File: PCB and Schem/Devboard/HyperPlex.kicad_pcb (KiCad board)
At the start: 2 copper layers, 23.2 x 47.8 mm, 27 parts, among them J1 USB_C_Receptacle_USB2.0_16P, Q1 2N3904, Q2 2N3904, Q3 2N3904, SW1 SW_Push, SW2 SW_SPDT, SW3 SW_SPDT, SW4 SW_Push, U1 CH32V203CxTx, U3 XC6206PxxxMR, U4 TP4056-42-ESOP8, U6 XC6206PxxxMR

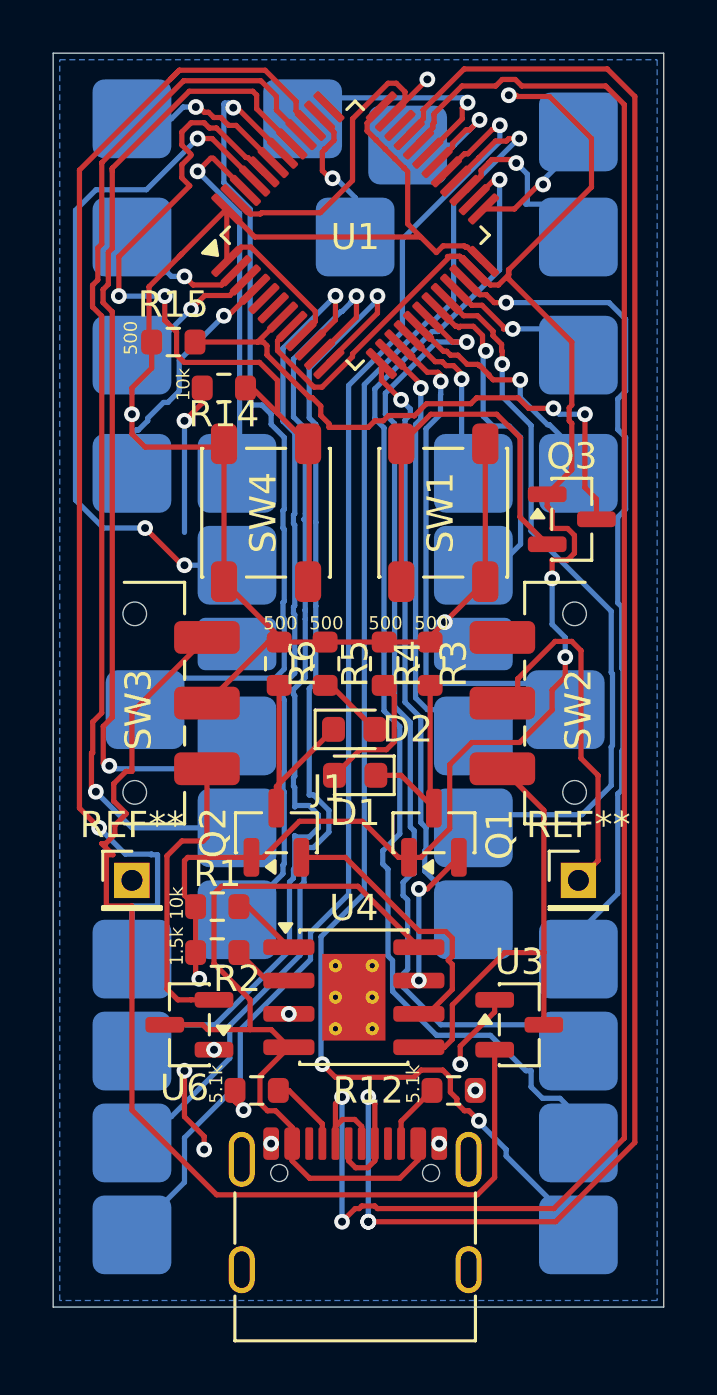
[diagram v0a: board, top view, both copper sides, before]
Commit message: Updated README, made Module 1 Schematic, started BOM
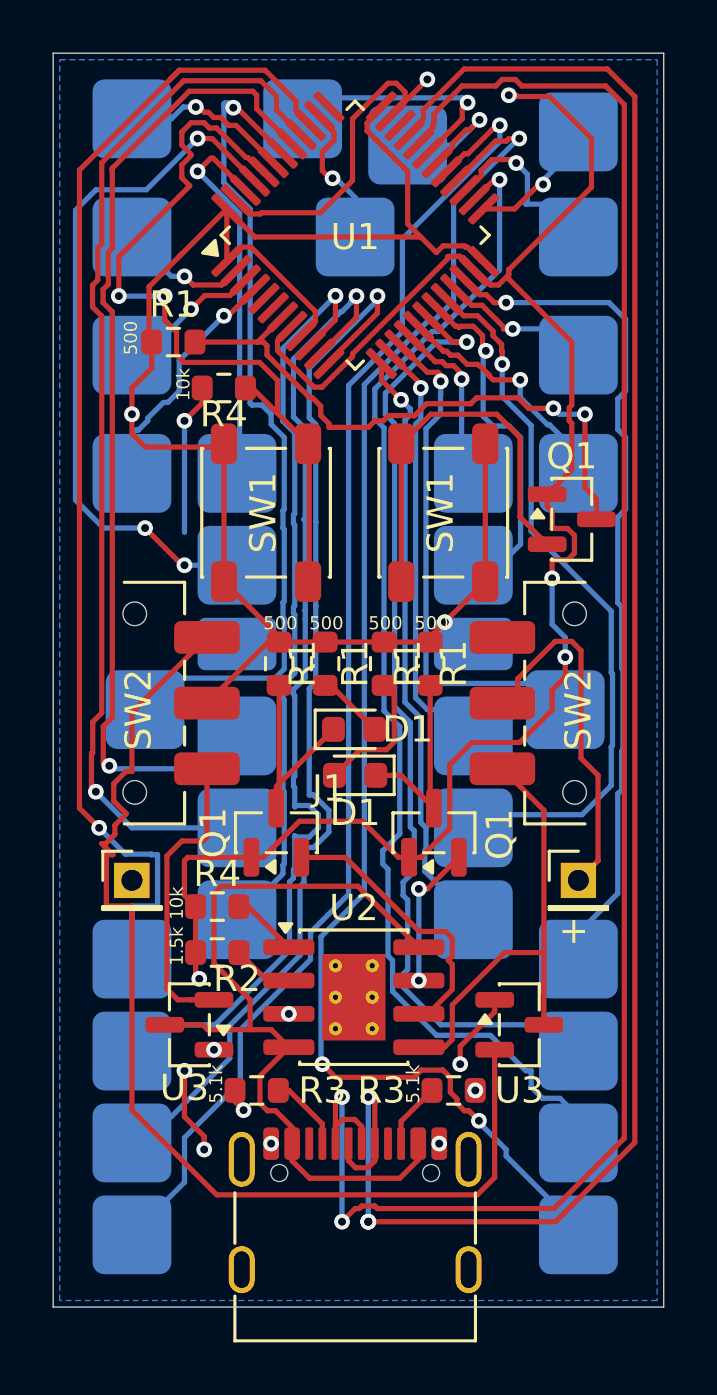
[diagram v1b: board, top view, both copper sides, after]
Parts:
- renumbered D2 to D1, Q2 to Q1, Q3 to Q1, R6 to R1, R5 to R1, R4 to R1, R15 to R1, R3 to R1, R12 to R3, R14 to R4, R1 to R4, SW4 to SW1, SW3 to SW2, U4 to U2, U6 to U3
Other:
- board text added: "+"
- board text added: "R3"
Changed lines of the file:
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@@
 			(drillshape 0)
 			(scaleselection 1)
-			(outputdirectory "./")
+			(outputdirectory "Final_Devboard_GBRs/")
 		)
 	)
@@
 		(descr "Diode SMD 0603 (1608 Metric), square (rectangular) end terminal, IPC-7351 nominal, (Body size source: http://www.tortai-tech.com/upload/download/2011102023233369053.pdf)")
 		(tags "diode")
-		(property "Reference" "D2"
+		(property "Reference" "D1"
 			(at 2.0375 0 0)
 			(layer "F.SilkS")
@@
 		(descr "Resistor SMD 0603 (1608 Metric), square (rectangular) end terminal, IPC-7351 nominal, (Body size source: IPC-SM-782 page 72, https://www.pcb-3d.com/wordpress/wp-content/uploads/ipc-sm-782a_amendment_1_and_2.pdf)")
 		(tags "resistor")
-		(property "Reference" "R14"
+		(property "Reference" "R4"
 			(at 0 1 0)
 			(layer "F.SilkS")
@@
 		(descr "SOT, 3 Pin (JEDEC TO-236 Var AB https://www.jedec.org/document_search?search_api_views_fulltext=TO-236)")
 		(tags "SOT TO_SOT_SMD")
-		(property "Reference" "Q2"
+		(property "Reference" "Q1"
 			(at 0 -2.4 90)
 			(layer "F.SilkS")
@@
 		(descr "Resistor SMD 0603 (1608 Metric), square (rectangular) end terminal, IPC-7351 nominal, (Body size source: IPC-SM-782 page 72, https://www.pcb-3d.com/wordpress/wp-content/uploads/ipc-sm-782a_amendment_1_and_2.pdf)")
 		(tags "resistor")
-		(property "Reference" "R6"
+		(property "Reference" "R1"
 			(at 0 -0.894105 90)
 			(layer "F.SilkS")
@@
 		(descr "C&K Components SPST SMD PTS647 Series 4.5mm Tact Switch, 3.8mm Height, see https://www.ckswitches.com/media/2567/pts647.pdf")
 		(tags "SPST Button Switch")
-		(property "Reference" "SW4"
+		(property "Reference" "SW1"
 			(at 0 -0.105895 90)
 			(layer "F.SilkS")
@@
 		(tags "SOT TO_SOT_SMD")
 		(property "Reference" "U3"
-			(at 0 -2.4 0)
+			(at 0 2.5 0)
 			(layer "F.SilkS")
 			(effects
@@
 		(descr "Resistor SMD 0603 (1608 Metric), square (rectangular) end terminal, IPC-7351 nominal, (Body size source: IPC-SM-782 page 72, https://www.pcb-3d.com/wordpress/wp-content/uploads/ipc-sm-782a_amendment_1_and_2.pdf)")
 		(tags "resistor")
-		(property "Reference" "R5"
+		(property "Reference" "R1"
 			(at 0 -1.144105 90)
 			(layer "F.SilkS")
@@
 		(descr "Resistor SMD 0603 (1608 Metric), square (rectangular) end terminal, IPC-7351 nominal, (Body size source: IPC-SM-782 page 72, https://www.pcb-3d.com/wordpress/wp-content/uploads/ipc-sm-782a_amendment_1_and_2.pdf)")
 		(tags "resistor")
-		(property "Reference" "R4"
+		(property "Reference" "R1"
 			(at 0 -0.894105 90)
 			(layer "F.SilkS")
@@
 		(descr "Resistor SMD 0603 (1608 Metric), square (rectangular) end terminal, IPC-7351 nominal, (Body size source: IPC-SM-782 page 72, https://www.pcb-3d.com/wordpress/wp-content/uploads/ipc-sm-782a_amendment_1_and_2.pdf)")
 		(tags "resistor")
-		(property "Reference" "R15"
+		(property "Reference" "R1"
 			(at 0 -1.43 0)
 			(layer "F.SilkS")
@@
 		(descr "Sub-miniature slide switch, right-angle, http://www.ckswitches.com/media/1422/js.pdf")
 		(tags "switch spdt")
-		(property "Reference" "SW3"
+		(property "Reference" "SW2"
 			(at 0.25 -0.144105 90)
 			(layer "F.SilkS")
@@
 		(descr "Resistor SMD 0603 (1608 Metric), square (rectangular) end terminal, IPC-7351 nominal, (Body size source: IPC-SM-782 page 72, https://www.pcb-3d.com/wordpress/wp-content/uploads/ipc-sm-782a_amendment_1_and_2.pdf)")
 		(tags "resistor")
-		(property "Reference" "R1"
+		(property "Reference" "R4"
 			(at 0 1.25 0)
 			(layer "F.SilkS")
@@
 			(at 0 -2.11 0)
 			(layer "F.SilkS")
+			(hide yes)
 			(effects
 				(font
@@
 		(descr "SOT, 3 Pin (JEDEC TO-236 Var AB https://www.jedec.org/document_search?search_api_views_fulltext=TO-236)")
 		(tags "SOT TO_SOT_SMD")
-		(property "Reference" "U6"
+		(property "Reference" "U3"
 			(at 0.187501 -2.4 0)
 			(layer "F.SilkS")
@@
 		(descr "SOIC, 8 Pin (http://www.allegromicro.com/~/media/Files/Datasheets/A4950-Datasheet.ashx#page=8)")
 		(tags "SOIC SO")
-		(property "Reference" "U4"
+		(property "Reference" "U2"
 			(at 0 -3.4 0)
 			(layer "F.SilkS")
@@
 			(at 0 -2.11 0)
 			(layer "F.SilkS")
+			(hide yes)
 			(effects
 				(font
@@
 		(descr "Resistor SMD 0603 (1608 Metric), square (rectangular) end terminal, IPC-7351 nominal, (Body size source: IPC-SM-782 page 72, https://www.pcb-3d.com/wordpress/wp-content/uploads/ipc-sm-782a_amendment_1_and_2.pdf)")
 		(tags "resistor")
-		(property "Reference" "R3"
+		(property "Reference" "R1"
 			(at 0 -0.894105 90)
 			(layer "F.SilkS")
@@
 		(descr "Resistor SMD 0603 (1608 Metric), square (rectangular) end terminal, IPC-7351 nominal, (Body size source: IPC-SM-782 page 72, https://www.pcb-3d.com/wordpress/wp-content/uploads/ipc-sm-782a_amendment_1_and_2.pdf)")
 		(tags "resistor")
-		(property "Reference" "R12"
-			(at -3.25 0 0)
+		(property "Reference" "R3"
+			(at -2.75 0 0)
 			(layer "F.SilkS")
 			(effects
@@
 		(descr "SOT, 3 Pin (JEDEC TO-236 Var AB https://www.jedec.org/document_search?search_api_views_fulltext=TO-236)")
 		(tags "SOT TO_SOT_SMD")
-		(property "Reference" "Q3"
+		(property "Reference" "Q1"
 			(at 0 -2.4 0)
 			(layer "F.SilkS")
@@
 		)
 	)
+	(gr_text "+"
+		(at 50.25 81.25 0)
+		(layer "F.SilkS")
+		(effects
+			(font
+				(size 1 1)
+				(thickness 0.1)
+			)
+			(justify left bottom)
+		)
+	)
+	(gr_text "R3"
+		(at 41.25 86.75 0)
+		(layer "F.SilkS")
+		(effects
+			(font
+				(size 1 1)
+				(thickness 0.15)
+			)
+		)
+	)
